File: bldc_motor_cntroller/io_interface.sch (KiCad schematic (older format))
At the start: 31 parts, among them J1 SM06B-SRSS-TB, J2 GENERIC 2.54P 06, J3 Conn_01x10, J4 Conn_01x05, J5 USB_B_Micro, J6 TC2030 Tag-connect, J7 SH-SM02B-SRSS, SW1 SW_Push, SW2 SW_Push, U1 TCAN332G

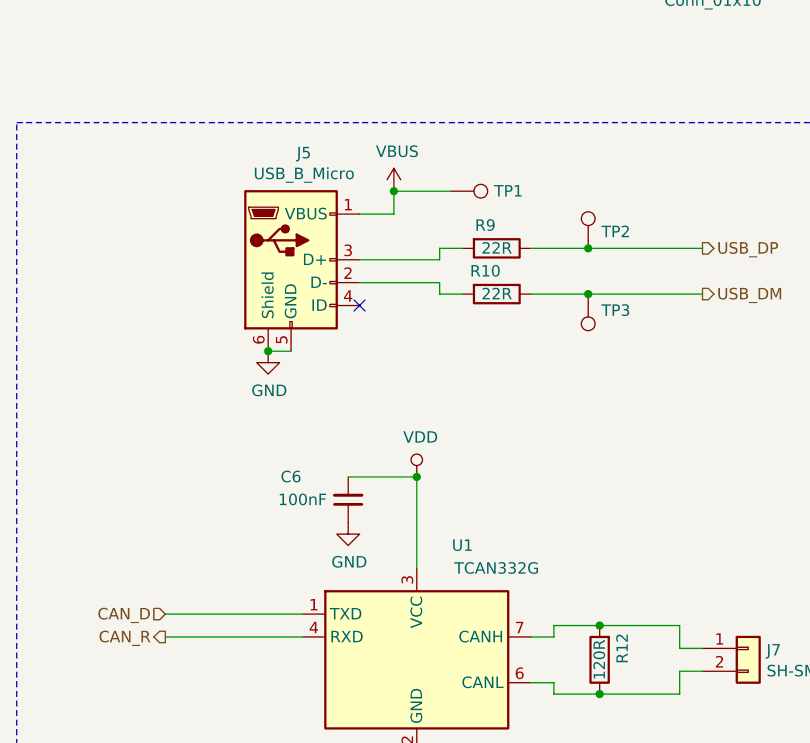
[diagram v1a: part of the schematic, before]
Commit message: added missing footprints.
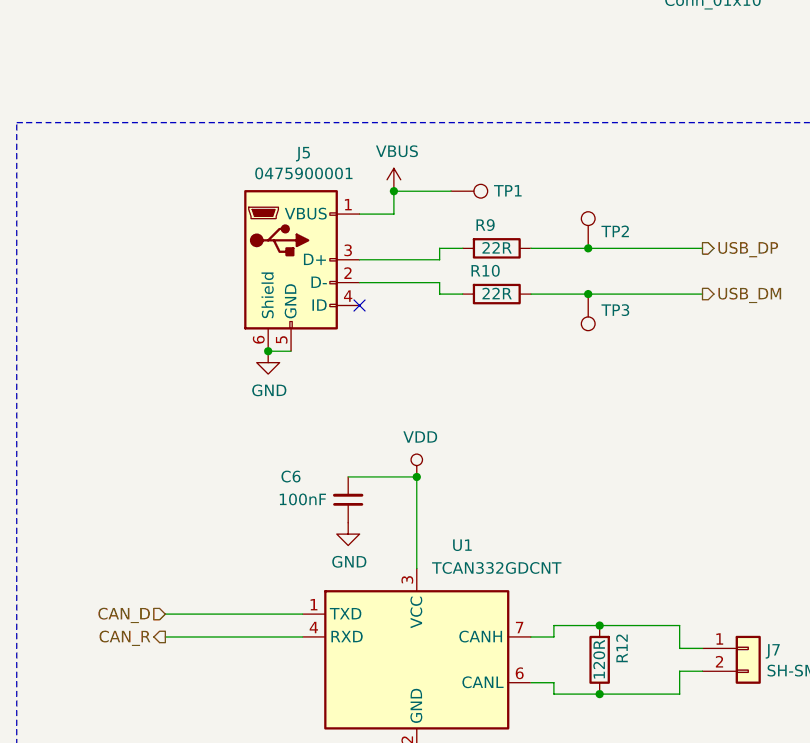
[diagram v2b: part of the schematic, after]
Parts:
- C1, C2, C3, C4, C5, C6: footprint (none) -> Capacitor_SMD:C_0402_1005Metric
- J3: footprint (none) -> Connector_PinHeader_2.54mm:PinHeader_1x10_P2.54mm_Vertical
- J4: footprint (none) -> Connector_PinHeader_2.54mm:PinHeader_1x05_P2.54mm_Vertical
- J5: value USB_B_Micro -> 0475900001; footprint (none) -> Connector_USB:USB_Micro-AB_Molex_47590-0001
- R1, R10, R11, R12, R2, R6, R7, R8, R9: footprint (none) -> Resistor_SMD:R_0402_1005Metric
- SW1, SW2: footprint (none) -> Button_Switch_SMD:SW_SPST_B3U-1000P
- TP1, TP2, TP3: footprint (none) -> TestPoint:TestPoint_Pad_D1.5mm
- U1: value TCAN332G -> TCAN332GDCNT; footprint (none) -> Package_TO_SOT_SMD:SOT-23-8
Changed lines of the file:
@@
 F 0 "J3" V 4225 3696 50  0000 C CNN
 F 1 "Conn_01x10" V 4316 3696 50  0000 C CNN
-F 2 "" H 4100 3750 50  0001 C CNN
+F 2 "Connector_PinHeader_2.54mm:PinHeader_1x10_P2.54mm_Vertical" H 4100 3750 50  0001 C CNN
 F 3 "~" H 4100 3750 50  0001 C CNN
 	1    4100 3750
@@
 F 0 "R1" V 2350 950 50  0000 C CNN
 F 1 "0R" V 2450 1000 50  0000 C CNN
-F 2 "" V 2380 1000 50  0001 C CNN
+F 2 "Resistor_SMD:R_0402_1005Metric" V 2380 1000 50  0001 C CNN
 F 3 "~" H 2450 1000 50  0001 C CNN
 	1    2450 1000
@@
 F 0 "C1" V 2500 1250 50  0000 C CNN
 F 1 "82pF" V 2400 1300 50  0000 C CNN
-F 2 "" H 2450 1150 50  0001 C CNN
+F 2 "Capacitor_SMD:C_0402_1005Metric" H 2450 1150 50  0001 C CNN
 F 3 "~" H 2450 1150 50  0001 C CNN
 	1    2450 1150
@@
 F 0 "R2" V 2350 1350 50  0000 C CNN
 F 1 "0R" V 2450 1400 50  0000 C CNN
-F 2 "" V 2380 1400 50  0001 C CNN
+F 2 "Resistor_SMD:R_0402_1005Metric" V 2380 1400 50  0001 C CNN
 F 3 "~" H 2450 1400 50  0001 C CNN
 	1    2450 1400
@@
 F 0 "C2" V 2450 1650 50  0000 C CNN
 F 1 "82pF" V 2350 1700 50  0000 C CNN
-F 2 "" H 2400 1550 50  0001 C CNN
+F 2 "Capacitor_SMD:C_0402_1005Metric" H 2400 1550 50  0001 C CNN
 F 3 "~" H 2400 1550 50  0001 C CNN
 	1    2400 1550
@@
 F 0 "R6" V 2350 2250 50  0000 C CNN
 F 1 "0R" V 2450 2300 50  0000 C CNN
-F 2 "" V 2380 2300 50  0001 C CNN
+F 2 "Resistor_SMD:R_0402_1005Metric" V 2380 2300 50  0001 C CNN
 F 3 "~" H 2450 2300 50  0001 C CNN
 	1    2450 2300
@@
 F 0 "C3" V 2450 2550 50  0000 C CNN
 F 1 "82pF" V 2350 2600 50  0000 C CNN
-F 2 "" H 2400 2450 50  0001 C CNN
+F 2 "Capacitor_SMD:C_0402_1005Metric" H 2400 2450 50  0001 C CNN
 F 3 "~" H 2400 2450 50  0001 C CNN
 	1    2400 2450
@@
 F 0 "R7" V 2350 2650 50  0000 C CNN
 F 1 "0R" V 2450 2700 50  0000 C CNN
-F 2 "" V 2380 2700 50  0001 C CNN
+F 2 "Resistor_SMD:R_0402_1005Metric" V 2380 2700 50  0001 C CNN
 F 3 "~" H 2450 2700 50  0001 C CNN
 	1    2450 2700
@@
 F 0 "C4" V 2450 2950 50  0000 C CNN
 F 1 "82pF" V 2350 3000 50  0000 C CNN
-F 2 "" H 2400 2850 50  0001 C CNN
+F 2 "Capacitor_SMD:C_0402_1005Metric" H 2400 2850 50  0001 C CNN
 F 3 "~" H 2400 2850 50  0001 C CNN
 	1    2400 2850
@@
 F 0 "R8" V 2350 3050 50  0000 C CNN
 F 1 "0R" V 2450 3100 50  0000 C CNN
-F 2 "" V 2380 3100 50  0001 C CNN
+F 2 "Resistor_SMD:R_0402_1005Metric" V 2380 3100 50  0001 C CNN
 F 3 "~" H 2450 3100 50  0001 C CNN
 	1    2450 3100
@@
 F 0 "C5" V 2450 3350 50  0000 C CNN
 F 1 "82pF" V 2350 3400 50  0000 C CNN
-F 2 "" H 2400 3250 50  0001 C CNN
+F 2 "Capacitor_SMD:C_0402_1005Metric" H 2400 3250 50  0001 C CNN
 F 3 "~" H 2400 3250 50  0001 C CNN
 	1    2400 3250
@@
 F 0 "J4" H 8130 4392 50  0000 L CNN
 F 1 "Conn_01x05" H 8130 4301 50  0000 L CNN
-F 2 "" H 8050 4350 50  0001 C CNN
+F 2 "Connector_PinHeader_2.54mm:PinHeader_1x05_P2.54mm_Vertical" H 8050 4350 50  0001 C CNN
 F 3 "~" H 8050 4350 50  0001 C CNN
 	1    8050 4350
@@
 F 0 "SW2" H 6050 5643 50  0000 C CNN
 F 1 "SW_Push" H 6050 5644 50  0001 C CNN
-F 2 "" H 6050 5650 50  0001 C CNN
+F 2 "Button_Switch_SMD:SW_SPST_B3U-1000P" H 6050 5650 50  0001 C CNN
 F 3 "~" H 6050 5650 50  0001 C CNN
 	1    6050 5450
@@
 F 0 "SW1" V 9450 5048 50  0000 L CNN
 F 1 "SW_Push" H 9450 5094 50  0001 C CNN
-F 2 "" H 9450 5100 50  0001 C CNN
+F 2 "Button_Switch_SMD:SW_SPST_B3U-1000P" H 9450 5100 50  0001 C CNN
 F 3 "~" H 9450 5100 50  0001 C CNN
 	1    9450 4900
@@
 F 0 "R11" V 9350 5250 50  0000 C CNN
 F 1 "10k" V 9450 5300 50  0000 C CNN
-F 2 "" V 9380 5300 50  0001 C CNN
+F 2 "Resistor_SMD:R_0402_1005Metric" V 9380 5300 50  0001 C CNN
 F 3 "~" H 9450 5300 50  0001 C CNN
 	1    9450 5300
@@
 P 2200 5100
 F 0 "J5" H 2257 5567 50  0000 C CNN
-F 1 "USB_B_Micro" H 2257 5476 50  0000 C CNN
-F 2 "" H 2350 5050 50  0001 C CNN
+F 1 "0475900001" H 2257 5476 50  0000 C CNN
+F 2 "Connector_USB:USB_Micro-AB_Molex_47590-0001" H 2350 5050 50  0001 C CNN
 F 3 "~" H 2350 5050 50  0001 C CNN
 	1    2200 5100
@@
 F 0 "R10" V 3000 5200 50  0000 C CNN
 F 1 "22R" V 3100 5250 50  0000 C CNN
-F 2 "" V 3030 5250 50  0001 C CNN
+F 2 "Resistor_SMD:R_0402_1005Metric" V 3030 5250 50  0001 C CNN
 F 3 "~" H 3100 5250 50  0001 C CNN
 	1    3100 5250
@@
 F 0 "R9" V 3000 5000 50  0000 C CNN
 F 1 "22R" V 3100 5050 50  0000 C CNN
-F 2 "" V 3030 5050 50  0001 C CNN
+F 2 "Resistor_SMD:R_0402_1005Metric" V 3030 5050 50  0001 C CNN
 F 3 "~" H 3100 5050 50  0001 C CNN
 	1    3100 5050
@@
 F 0 "TP1" V 2900 4988 50  0000 L CNN
 F 1 "TestPoint" V 2945 4988 50  0001 L CNN
-F 2 "" H 3100 4800 50  0001 C CNN
+F 2 "TestPoint:TestPoint_Pad_D1.5mm" H 3100 4800 50  0001 C CNN
 F 3 "~" H 3100 4800 50  0001 C CNN
 	1    2900 4800
@@
 F 0 "TP2" H 3558 5122 50  0000 L CNN
 F 1 "TestPoint" V 3545 5238 50  0001 L CNN
-F 2 "" H 3700 5050 50  0001 C CNN
+F 2 "TestPoint:TestPoint_Pad_D1.5mm" H 3700 5050 50  0001 C CNN
 F 3 "~" H 3700 5050 50  0001 C CNN
 	1    3500 5050
@@
 F 0 "TP3" H 3442 5322 50  0000 R CNN
 F 1 "TestPoint" V 3545 5438 50  0001 L CNN
-F 2 "" H 3700 5250 50  0001 C CNN
+F 2 "TestPoint:TestPoint_Pad_D1.5mm" H 3700 5250 50  0001 C CNN
 F 3 "~" H 3700 5250 50  0001 C CNN
 	1    3500 5250
@@
 F 0 "C6" H 2700 6050 50  0000 C CNN
 F 1 "100nF" H 2650 6150 50  0000 C CNN
-F 2 "" H 2450 6150 50  0001 C CNN
+F 2 "Capacitor_SMD:C_0402_1005Metric" H 2450 6150 50  0001 C CNN
 F 3 "~" H 2450 6150 50  0001 C CNN
 	1    2450 6150
@@
 P 2750 6850
 F 0 "U1" H 2950 7350 50  0000 C CNN
-F 1 "TCAN332G" H 3100 7250 50  0000 C CNN
-F 2 "" H 2750 6350 50  0001 C CIN
+F 1 "TCAN332GDCNT" H 3100 7250 50  0000 C CNN
+F 2 "Package_TO_SOT_SMD:SOT-23-8" H 2750 6350 50  0001 C CIN
 F 3 "http://www.ti.com/lit/ds/symlink/tcan337.pdf" H 2750 6850 50  0001 C CNN
 	1    2750 6850
@@
 F 0 "R12" V 3450 6800 50  0000 C CNN
 F 1 "120R" V 3550 6850 50  0000 C CNN
-F 2 "" V 3480 6850 50  0001 C CNN
+F 2 "Resistor_SMD:R_0402_1005Metric" V 3480 6850 50  0001 C CNN
 F 3 "~" H 3550 6850 50  0001 C CNN
 	1    3550 6850

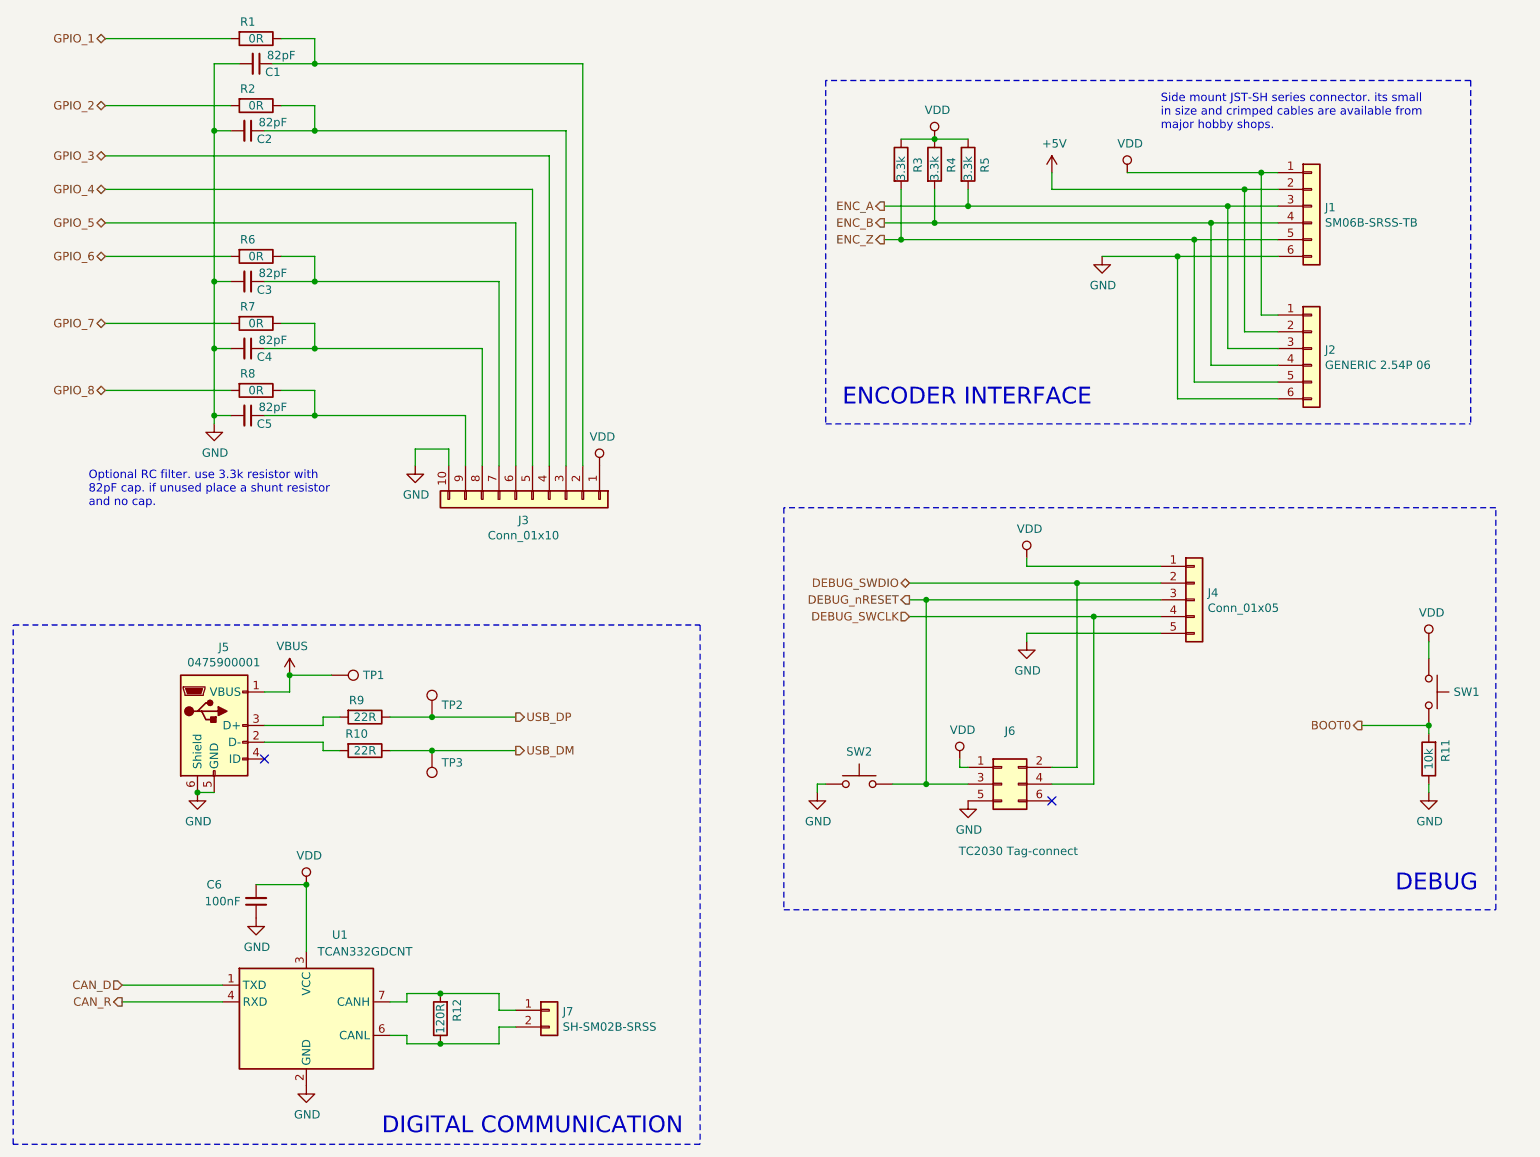
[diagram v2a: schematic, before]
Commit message: combined 2.54p connectors. changed diode footprint.
Signed-off-by: azmat bilal <azmat.bilal@outlook.com>
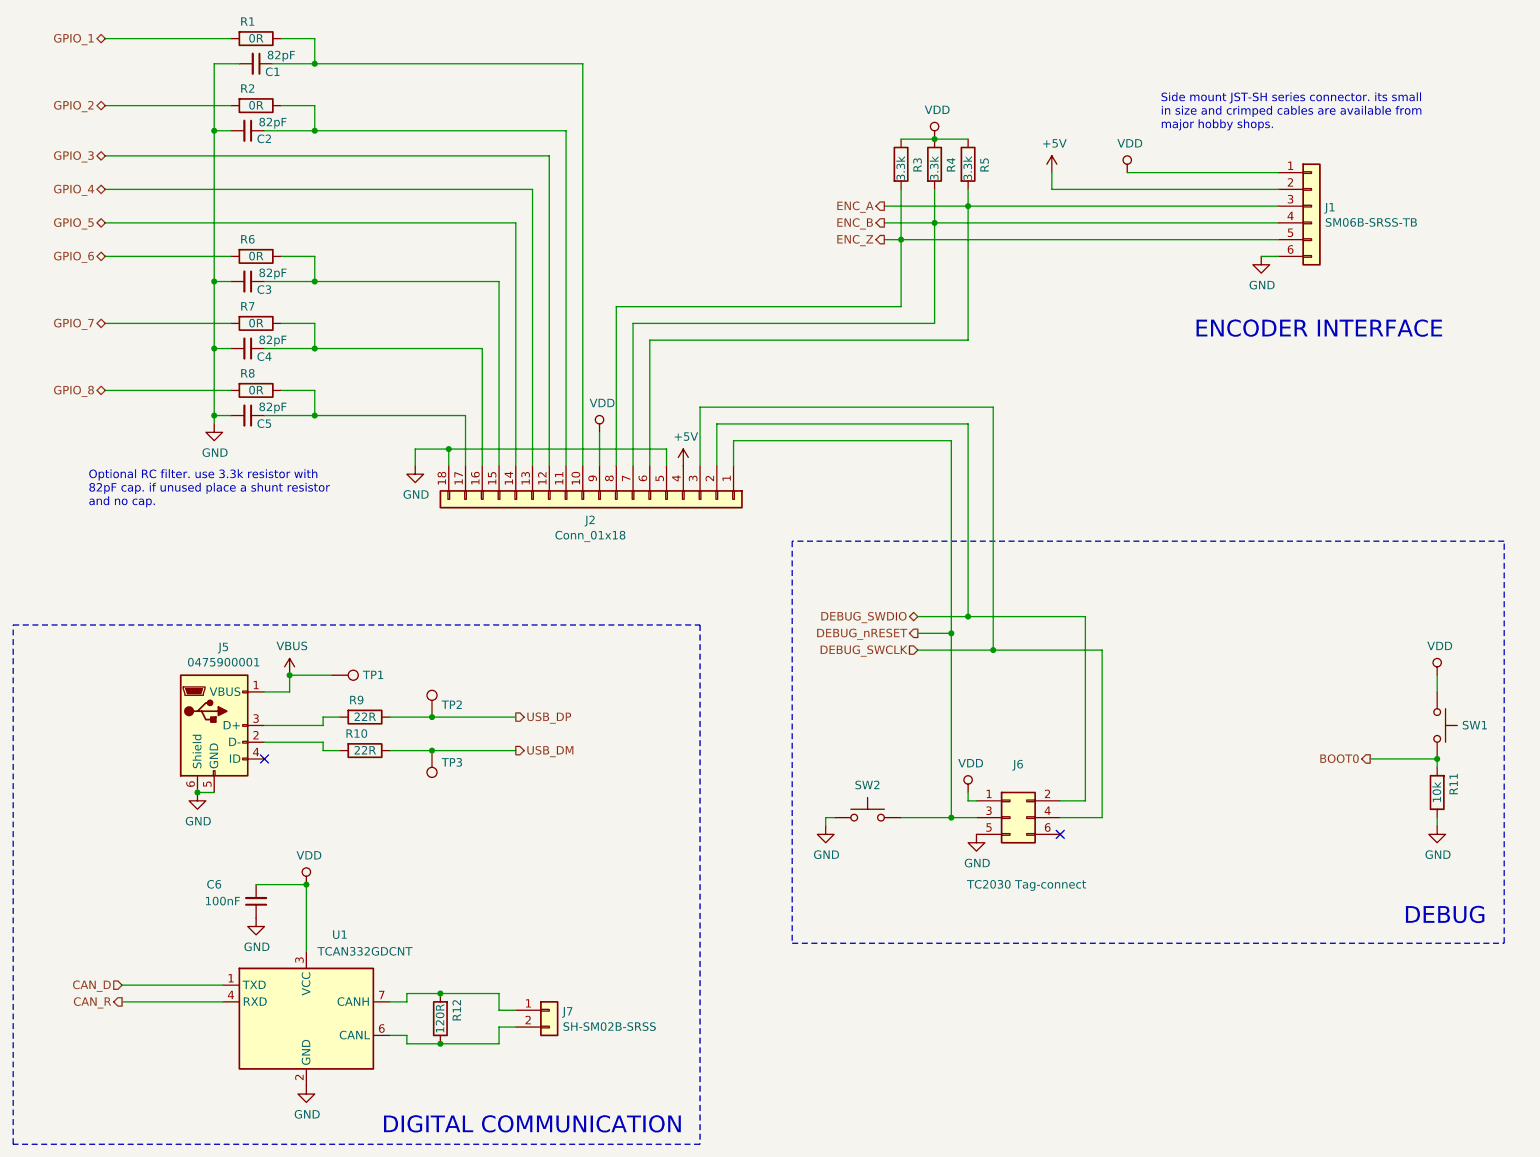
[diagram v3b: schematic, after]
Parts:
- removed J2: GENERIC 2.54P 06, Connector_PinHeader_2.54mm:PinHeader_1x06_P2.54mm_Horizontal, symbol Connector_Generic:Conn_01x06
- removed J3: Conn_01x10, Connector_PinHeader_2.54mm:PinHeader_1x10_P2.54mm_Vertical, symbol Connector_Generic:Conn_01x10
- removed J4: Conn_01x05, Connector_PinHeader_2.54mm:PinHeader_1x05_P2.54mm_Vertical, symbol Connector_Generic:Conn_01x05
- added J2: Conn_01x18, Connector_PinHeader_2.54mm:PinHeader_1x18_P2.54mm_Horizontal, symbol Connector_Generic:Conn_01x18
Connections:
- net +5V: now also J2.4 (Pin_4)
- net DEBUG_SWCLK: now also J2.3 (Pin_3)
- net DEBUG_SWDIO: now also J2.2 (Pin_2)
- net DEBUG_nRESET: now also J2.1 (Pin_1)
- net ENC_A: now also J2.6 (Pin_6)
- net ENC_B: now also J2.7 (Pin_7)
- net ENC_Z: now also J2.8 (Pin_8)
- net GND: now also J2.18 (Pin_18), J2.5 (Pin_5)
- net GPIO_3: now also J2.12 (Pin_12)
- net GPIO_4: now also J2.13 (Pin_13)
- net GPIO_5: now also J2.14 (Pin_14)
- net VDD: now also J2.9 (Pin_9)
- net at C1.1, R1.1: now also J2.10 (Pin_10)
- net at C2.1, R2.1: now also J2.11 (Pin_11)
- net at C3.1, R6.1: now also J2.15 (Pin_15)
- net at C4.1, R7.1: now also J2.16 (Pin_16)
- net at C5.1, R8.1: now also J2.17 (Pin_17)
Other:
- moved on the sheet: J6, R11, SW1, SW2
